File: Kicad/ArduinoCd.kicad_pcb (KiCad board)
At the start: 2 copper layers, 100 x 100 mm, 104 parts, among them J1 Conn_01x02, J10 OLED, J11 Conn_01x02, J12 Conn_01x02, J13 Conn_01x02, J14 Conn_01x02, J15 IDE, J16 12v-IN, J17 LineOut, J2 A4-A5, J3 Conn_01x02, J4 fcr684204t, J5 Conn_01x02, J6 Conn_01x02, J7 IR SENSE, J8 S/PDIF-IN0, J9 S/PDIF-IN1, Q1 2N7002, Q2 2N7002, Q3 2N7002, Q4 2N7002, SW1 Stop, SW2 Play, SW3 Pause, SW4 PrevTrack, SW5 NextTrack, SW6 FastForward, SW7 Rewind, SW8 Eject, U1 PCA9555PW, U2 PCA9555PW, U3 WM8805, U4 AMS1117-3.3, U5 PCM5102, U6 LT3042, U7 AMS1117-5.0, Y1 12MHz

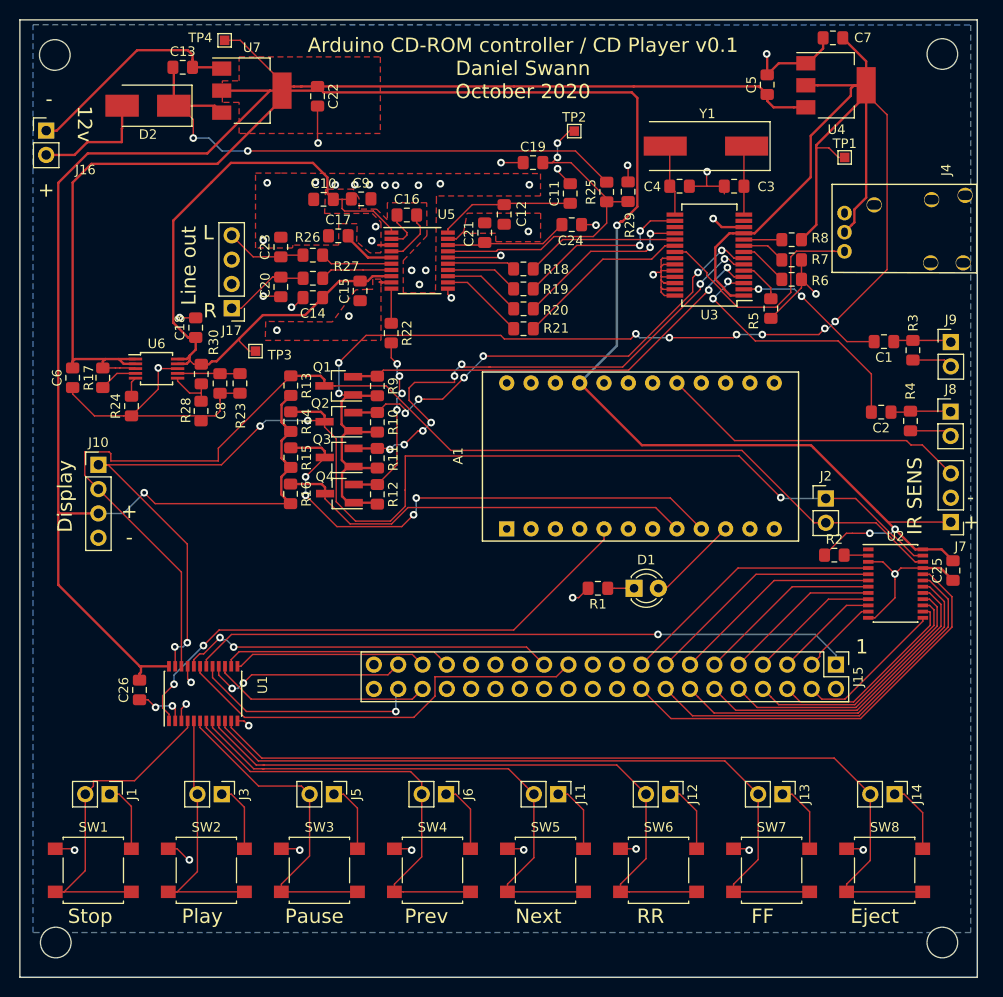
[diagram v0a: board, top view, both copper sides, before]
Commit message: added my version of pcb (includes power connector and bodge wire fix, but wm8805 doesnt work)
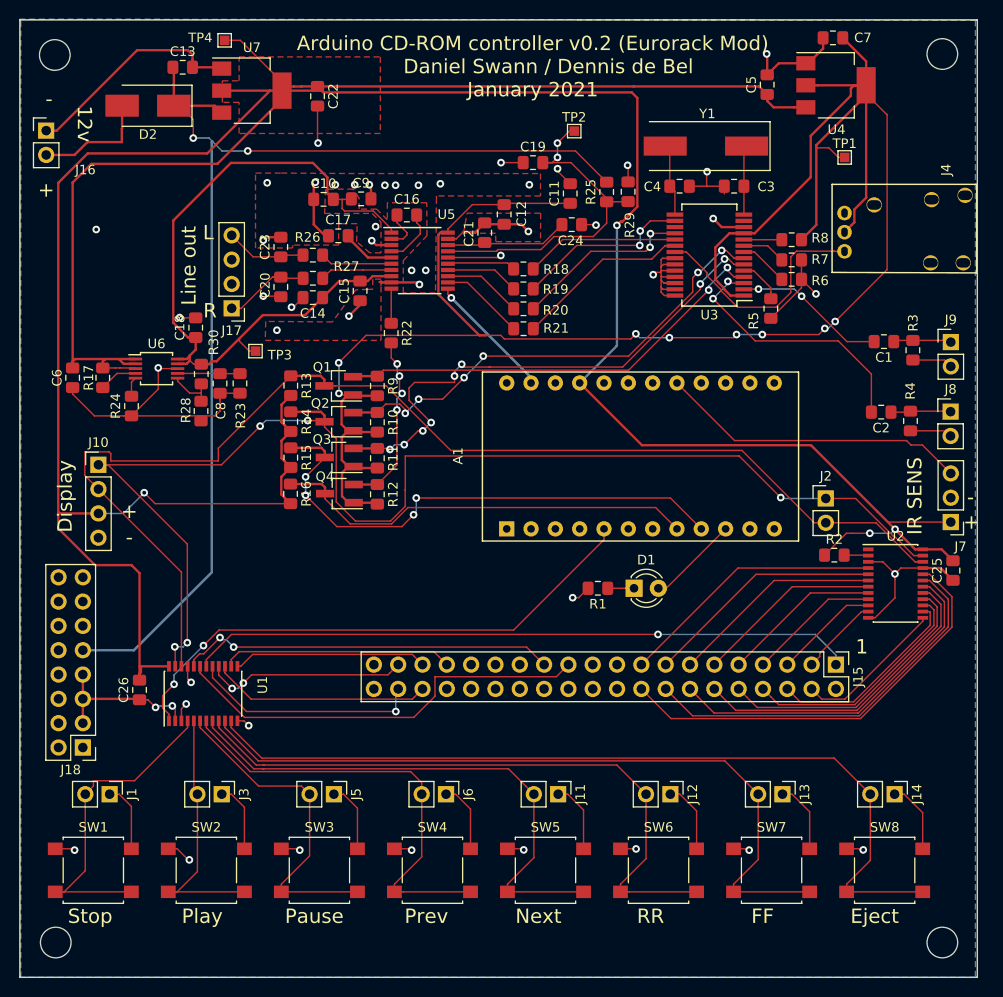
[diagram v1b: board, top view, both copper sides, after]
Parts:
- added J18: Eurorack_02x08, Connector_PinHeader_2.54mm:PinHeader_2x08_P2.54mm_Vertical, F.Cu at (138.4, 87.6)
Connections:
- A1 pad 1: (no net) -> Net-(A1-Pad1)
- A1 pad 11: (no net) -> Net-(A1-Pad11)
- A1 pad 12: (no net) -> Net-(A1-Pad12)
- A1 pad 13: (no net) -> Net-(A1-Pad13)
- A1 pad 14: (no net) -> Net-(A1-Pad14)
- A1 pad 15: (no net) -> Net-(A1-Pad15)
- A1 pad 16: (no net) -> Net-(A1-Pad16)
- A1 pad 18: (no net) -> Net-(A1-Pad18)
- A1 pad 19: (no net) -> Net-(A1-Pad19)
- A1 pad 2: (no net) -> Net-(A1-Pad2)
- A1 pad 20: (no net) -> Net-(A1-Pad20)
- A1 pad 22: (no net) -> Net-(A1-Pad22)
- A1 pad 24: (no net) -> Net-(A1-Pad24)
- A1 pad 3: (no net) -> Net-(A1-Pad3)
- A1 pad 6: (no net) -> Net-(A1-Pad6)
- A1 pad 7: (no net) -> Net-(A1-Pad7)
- C11 pad 1: Net-(C11-Pad1) -> 3v3
- C12 pad 2: Net-(C11-Pad1) -> 3v3
- J15 pad 20: (no net) -> Net-(J15-Pad20)
- J15 pad 21: (no net) -> Net-(J15-Pad21)
- J15 pad 27: (no net) -> Net-(J15-Pad27)
- J15 pad 28: (no net) -> Net-(J15-Pad28)
- J15 pad 29: (no net) -> Net-(J15-Pad29)
- J15 pad 31: (no net) -> Net-(J15-Pad31)
- J15 pad 32: (no net) -> Net-(J15-Pad32)
- J15 pad 34: (no net) -> Net-(J15-Pad34)
- J15 pad 39: (no net) -> Net-(J15-Pad39)
- J4 pad 1: (no net) -> Net-(J4-Pad1)
- J4 pad 2: (no net) -> Net-(J4-Pad2)
- J4 pad 3: (no net) -> Net-(J4-Pad3)
- J4 pad 4: (no net) -> Net-(J4-Pad4)
- J4 pad 5: (no net) -> Net-(J4-Pad5)
- U2 pad 1: (no net) -> Net-(U2-Pad1)
- U3 pad 13: (no net) -> Net-(U3-Pad13)
- U3 pad 17: (no net) -> Net-(U3-Pad17)
- U5 pad 20: Net-(C11-Pad1) -> 3v3
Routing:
- net 12v: track 59.0 -> 120.9 mm
- net AGND: track 238.0 -> 284.8 mm, vias 50 -> 51
- net 3v3: track 195.9 -> 224.3 mm
- net Net-(C11-Pad1): track 14.3 -> 0.00 mm
- net 5v: track 388.1 -> 391.7 mm
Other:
- board text added: "Arduino CD-ROM controller v0.2 (Eurorack Mod) Daniel Swann / Dennis de Bel January 2021"
- board text removed: "Arduino CD-ROM controller / CD Player v0.1 Daniel Swann October 2020"
